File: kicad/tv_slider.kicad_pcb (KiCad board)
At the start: 2 copper layers, 100.6 x 75.2 mm, 96 parts, among them J1 MC 1,5/2-G-3.81, J2 MC 1,5/6-G-3.81, J3 MC 1,5/4-G-3.81, J4 MC 1,5/3-G-3.81, J5 MC 1,5/3-G-3.81, J6 MC 1,5/3-G-3.81, J7 MC 1,5/3-G-3.81, J8 Conn_01x05, Q1 CSD19537Q3, Q2 BSS138, U1 TPS26632RGE, U2 LMR33610ADDAR, U3 ESP32-C6-DEVKITC-1-N8, U4 DRV8452SPWPR, U5 ISL3280ExHZ, U6 LS7184N-S, U7 ISL3280ExHZ

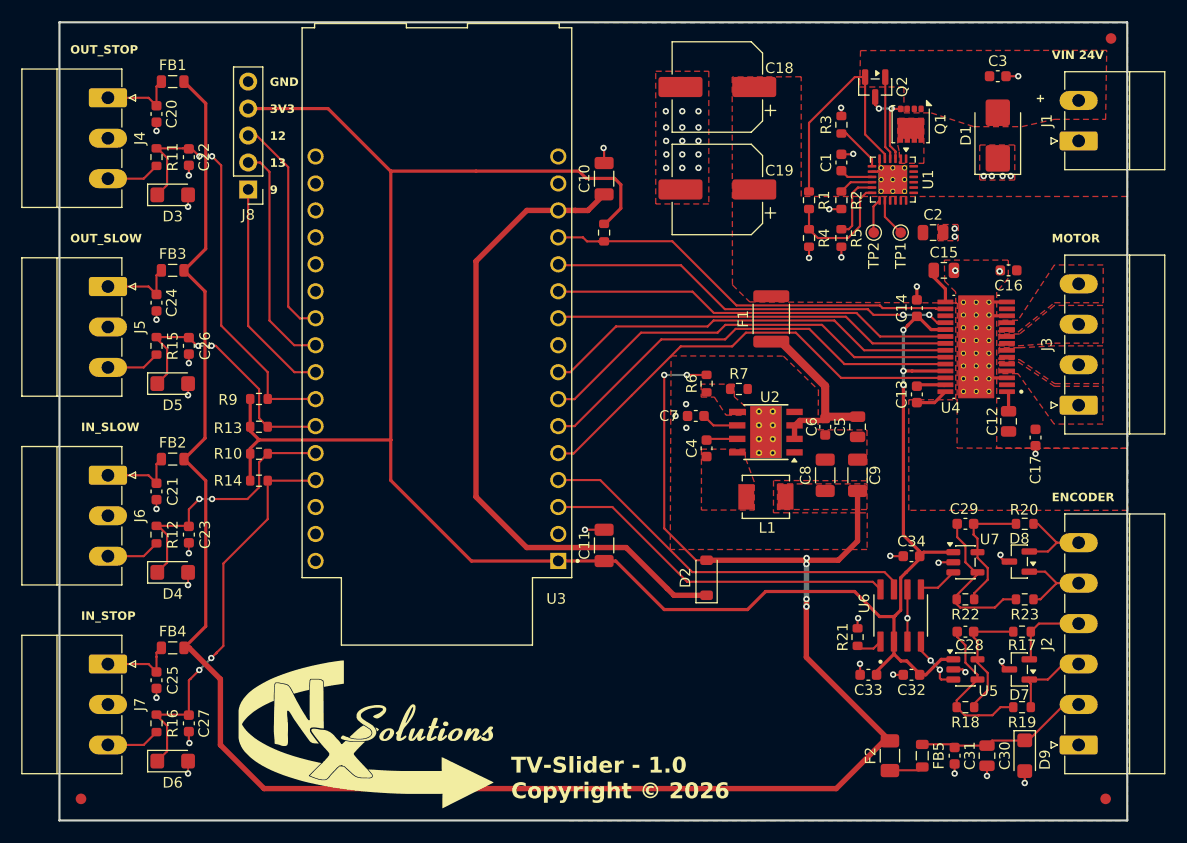
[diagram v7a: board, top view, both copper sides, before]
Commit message: Updated to use more of JCLPCB's basic components. Added extra field "FT Rotation Offset" to get the correct orientation for placement at JCLPCB.
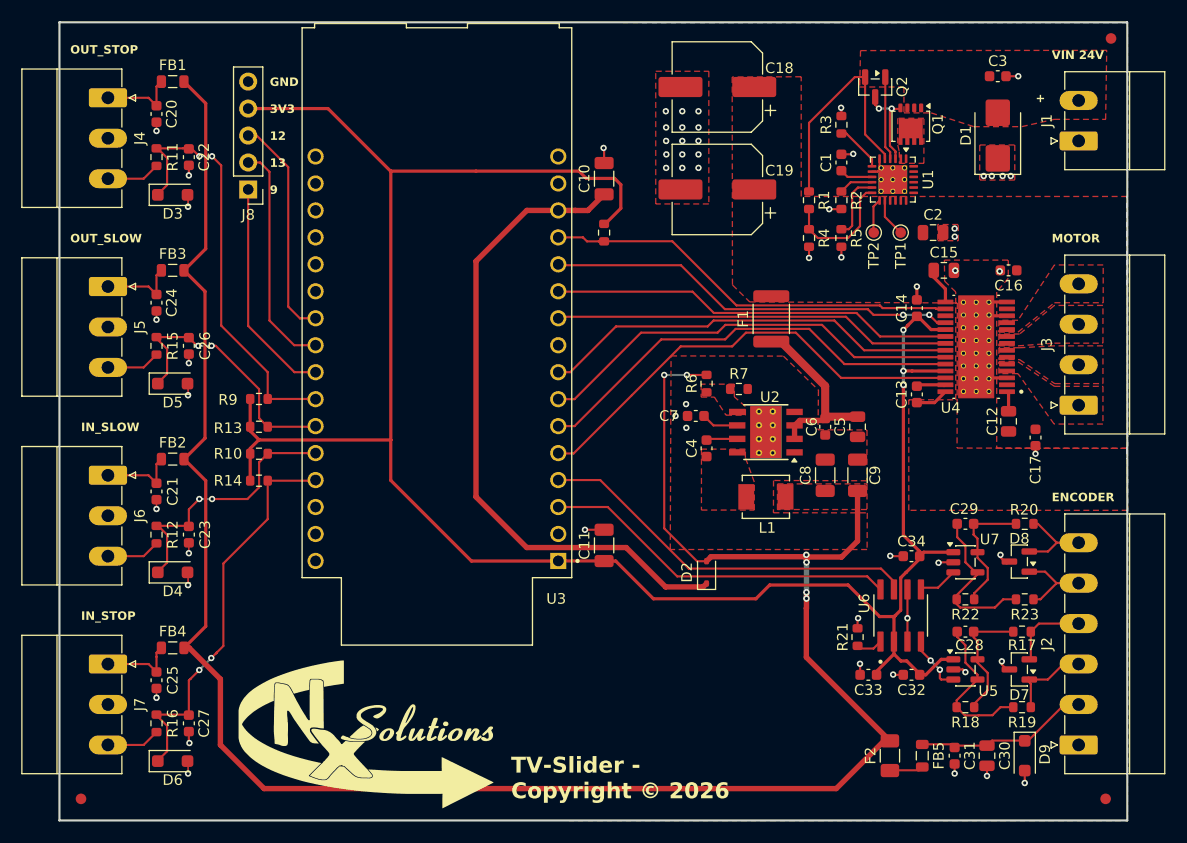
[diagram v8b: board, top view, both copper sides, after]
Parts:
- D2: value 1N5819HW-7-F -> 1N5819WS; footprint Diode_SMD:D_SOD-123 -> Diode_SMD:D_SOD-323
- D3, D4, D5, D6: value SMF5V0A -> SMF5.0A; footprint Diode_SMD:D_SMF -> Diode_SMD:D_SOD-123F
- D7, D8: value SM712_SOT23 -> SM712
- D9: value SMF6V0A -> SMF6.0A; footprint Diode_SMD:D_SMF -> Diode_SMD:D_SOD-123F
- Q1: value CSD19537Q3 -> BUK9M34-100EX; footprint Package_SON:VSON-8_3.3x3.3mm_P0.65mm_NexFET -> Package_TO_SOT_SMD:LFPAK33
- R2: value 9.09k -> 9.1k
- moved D2 0.51 mm to (142.7, 108.2)
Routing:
- net +5V: track 201.5 -> 202.3 mm
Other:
- board text added: "TV-Slider - ${REVISION} Copyright © 2026"
- board text removed: "TV-Slider - 1.0 Copyright © 2026"
